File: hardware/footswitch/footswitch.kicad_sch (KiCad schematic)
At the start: 4 parts, among them J1 Conn_02x05_Counter_Clockwise

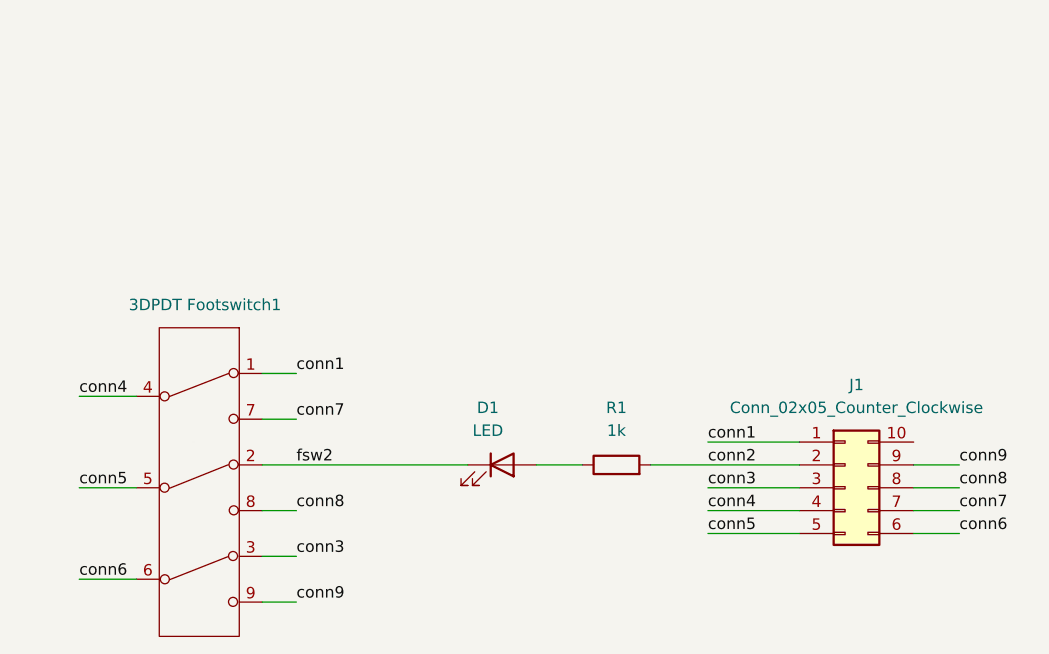
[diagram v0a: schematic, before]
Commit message: Adapt board for pcb mounted footswitches
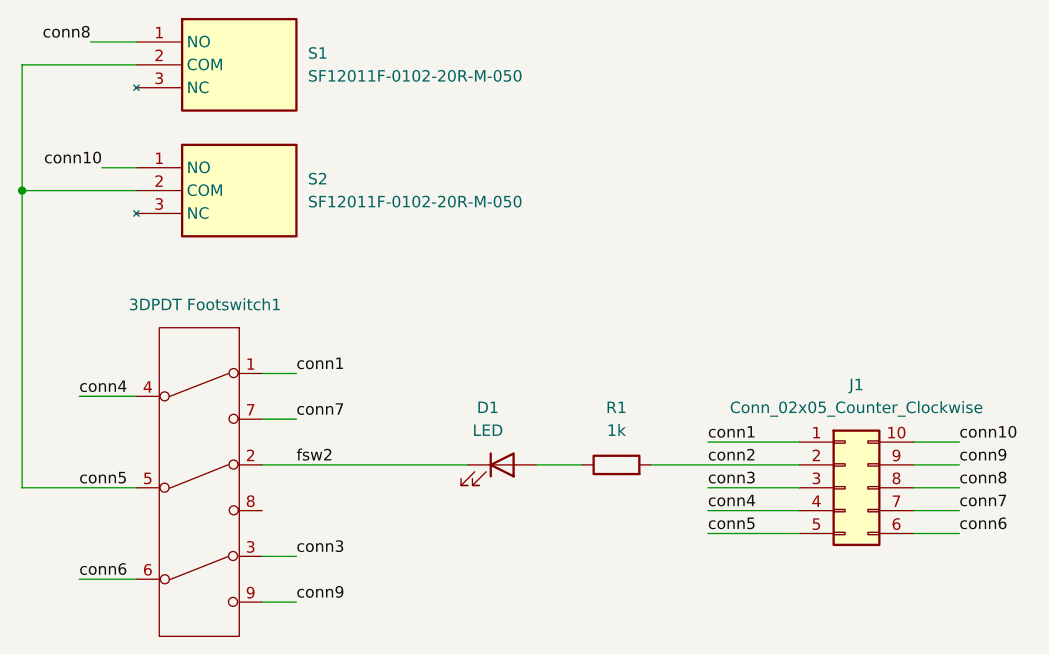
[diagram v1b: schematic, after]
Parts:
- added S1, S2: SF12011F-0102-20R-M-050, pcb switch:SF12011F010220RM050, symbol SF12011F-0102-20R-M-050:SF12011F-0102-20R-M-050
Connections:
- net conn5: now also S1.2 (COM), S2.2 (COM)
- net conn8: now also S1.1 (NO); no longer 3DPDT Footswitch1.8 (G)
- net conn10: now reaches J1.10 (Pin_10)
- net conn10: now also S2.1 (NO)
